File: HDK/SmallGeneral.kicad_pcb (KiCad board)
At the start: 2 copper layers, 80 x 50 mm, 45 parts, among them J101 PHD_02x04V-H, J102 USB_C, J103 PH_01x05V-H, J104 Conn_01x08, J105 PH_01x05V-H, J106 PH_01x05V-H, J107 PHD_02x04V-H, J108 PHD_02x04V-H, J109 Conn_01x08, SW101 SW_Push, SW102 SW_Push, U101 STM32F072CBTx, U102 TJA1042T-3, U103 AMS1117-3.3

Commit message: updated rev3
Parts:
- removed the G*** at (156.2, 122.5)
- removed H101, H102, H103, H104: MountingHole_4.3mm_M4_DIN965_Pad_TopBottom, MountingHole:MountingHole_4.3mm_M4_DIN965_Pad_TopBottom
- removed the J101 at (108.0, 132.6)
- removed J103, J105, J106: PH_01x05V-H, NVF-Kicad:PH_01x05H-H
- removed J104, J109: Conn_01x08, Connector_PinHeader_2.54mm:PinHeader_1x08_P2.54mm_Vertical
- removed J107, J108: PHD_02x04V-H, NVF-Kicad:PHD_02x04H-H
- removed SWD101: SWD_Breakout_Minimal, NVF-Kicad:PH_01x05H-H
- removed kibuzzard-65C10781: G***, kibuzzard-65C10781
- removed kibuzzard-65C107BB: G***, kibuzzard-65C107BB
- added C110: 100n, Capacitor_SMD:C_0603_1608Metric, F.Cu at (156.7, 138.5)
- added C113: 2u2, Capacitor_SMD:C_0805_2012Metric, F.Cu at (167.3, 118.9)
- added C114: 2u2, Capacitor_SMD:C_0805_2012Metric, F.Cu at (167.3, 116.6)
- added D101: GREEN, LED_SMD:LED_0603_1608Metric, F.Cu at (154.8, 133.3)
- added D102: RED, LED_SMD:LED_0603_1608Metric, F.Cu at (152.2, 133.3)
- added D103: BLUE, LED_SMD:LED_0603_1608Metric, F.Cu at (149.5, 133.3)
- added R103: 10k, Resistor_SMD:R_0603_1608Metric, F.Cu at (156.7, 140.2)
- added R104: 1k, Resistor_SMD:R_0603_1608Metric, F.Cu at (156.7, 141.8)
- added R105: 200, Resistor_SMD:R_0603_1608Metric, F.Cu at (154.7, 129.9)
- added R106: 200, Resistor_SMD:R_0603_1608Metric, F.Cu at (152.2, 129.9)
- added R107: 200, Resistor_SMD:R_0603_1608Metric, F.Cu at (149.5, 129.9)
- added R110: 10k, Resistor_SMD:R_0603_1608Metric, F.Cu at (160.8, 140.4)
- added R111: 1k, Resistor_SMD:R_0603_1608Metric, F.Cu at (160.8, 142.1)
- added RV102: 10k, NVF-Kicad:RV_Bourns_3362, F.Cu at (129.9, 121.9)
- added SG101: ~, NVF-OwnParts:Small-General Actual, F.Cu at (140.0, 125.0)
- added SW103: SW_Push, NVF-Kicad:PushBtn_TS-1187A-B-A-B, F.Cu at (159.8, 146.2)
- added TP102: TestPoint, TestPoint:TestPoint_Pad_2.5x2.5mm, F.Cu at (116.0, 110.4)
- added TP103: TestPoint, TestPoint:TestPoint_Pad_2.5x2.5mm, F.Cu at (177.2, 122.5)
- added U104: AMS1117-5.0, Package_TO_SOT_SMD:SOT-223-3_TabPin2, F.Cu at (173.9, 116.7)
- added kibuzzard-65CCCADD: G***, kibuzzard-65CCCADD, F.Cu at (164.2, 123.9)
- added kibuzzard-65CCCB35: G***, kibuzzard-65CCCB35, B.Cu at (139.3, 125.1)
- moved R101 8.88 mm to (128.6, 117.2), turned to 0 degrees
- moved D104 6.83 mm to (166.6, 138.2)
- moved C103 2.35 mm to (129.9, 128.3), turned to 180 degrees
- moved kibuzzard-65C10821 1.98 mm to (146.4, 135.0)
- moved kibuzzard-65C10836 1.98 mm to (144.0, 130.0)
- renumbered C111 to C109, C109 to C111, C110 to C112, D101 to D104, D102 to D105, D103 to D106, J102 to J101, R105 to R102, R103 to R108, R104 to R109
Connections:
- net BOOT0 renamed /BOOT0
- C109 pad 1: NRST -> /NRST
- R101 pad 1: NRST -> +3V3
- R101 pad 2: +3V3 -> /NRST
- SW102 pad 1: NRST -> /NRST
- U101 pad 10: unconnected-(U101-PA0-Pad10) -> /A0_MCU
- U101 pad 11: /A0_MCU -> /A1_MCU
- U101 pad 19: unconnected-(U101-PB1-Pad19) -> /V_{SENSE}
- U101 pad 20: unconnected-(U101-PB2-Pad20) -> /USR_BTN
- U101 pad 21: unconnected-(U101-PB10-Pad21) -> /USR_LED
- U101 pad 7: NRST -> /NRST
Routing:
- net NRST: track 71.4 -> 0.00 mm, vias 5 -> 0
- net /NRST: track 0.00 -> 68.1 mm, vias 0 -> 5
- net +5V: track 102.1 -> 154.3 mm, vias 2 -> 4
- net /A1_MCU: track 0.00 -> 43.8 mm, vias 0 -> 2
- net VCC: track 63.8 -> 98.5 mm, vias 2 -> 4
- net /USR_LED: track 0.00 -> 32.1 mm, vias 0 -> 2
- net /V_{SENSE}: track 0.00 -> 29.9 mm, vias 0 -> 2
- net /A1: track 0.00 -> 26.8 mm
- net /USR_BTN: track 0.00 -> 25.1 mm
- net Net-(R104-Pad2): track 0.00 -> 8.75 mm
- net VBUS: track 21.9 -> 14.6 mm
- net GND: track 44.8 -> 51.4 mm, vias 23 -> 35
- net +3V3: track 227.7 -> 233.8 mm, vias 8 -> 9
- net /SPI_MOSI: track 26.6 -> 21.1 mm
- net /SPI_SCLK: track 22.0 -> 18.0 mm
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- added copper zone on F.Cu, net +5V
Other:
- board text added: "3V3"
- board text added: "5V"
- board text added: "A0_T"
- board text added: "A1_T"
- board text added: "B"
- board text added: "BOOT"
- board text added: "G"
- board text added: "NRST"
- board text added: "Rev3"
- board text added: "Scott CJX NVF"
- board text added: "USR"
- board text removed: "A0"
- board text removed: "CAN"
- board text removed: "CAN INTR"
- board text removed: "I2C"
- board text removed: "Rev1"
- board text removed: "SPI"
- board text removed: "SWD"
- board text removed: "UART"

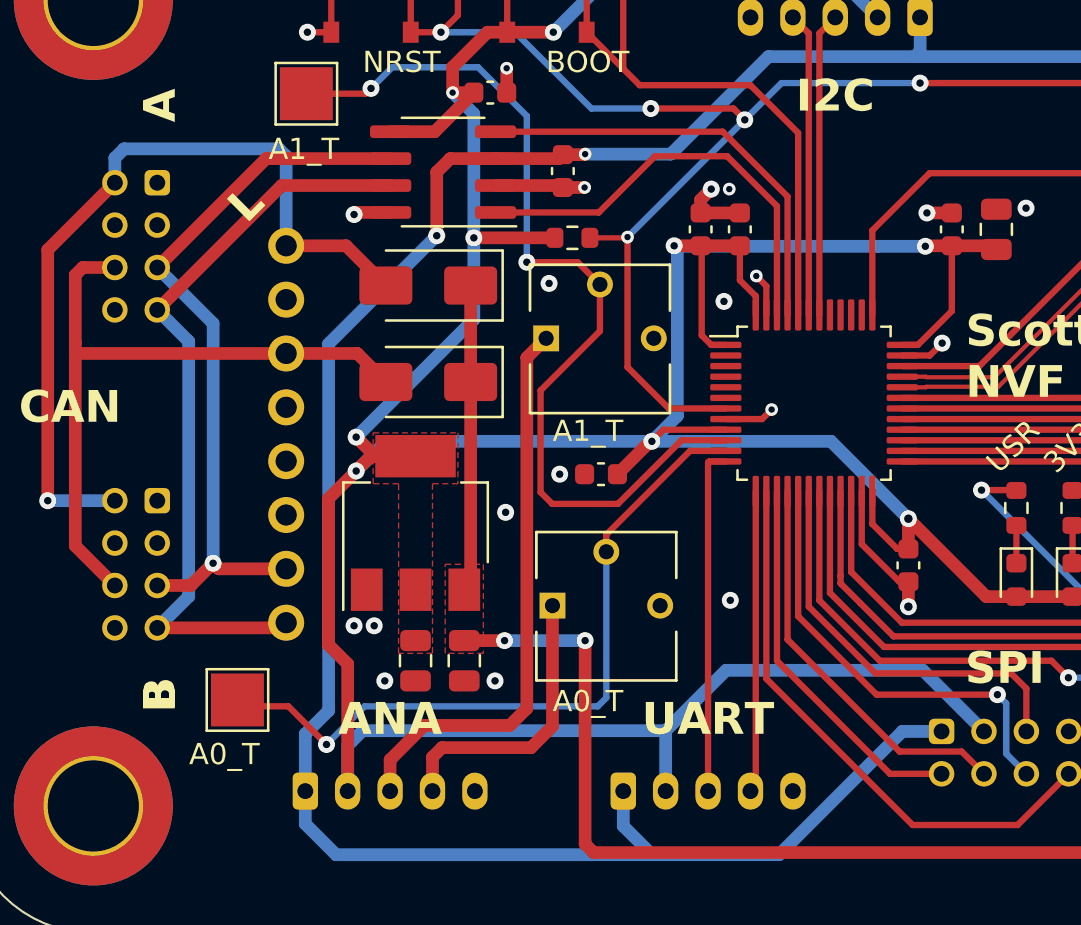
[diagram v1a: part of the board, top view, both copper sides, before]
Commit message: updated Trim Pot Switch
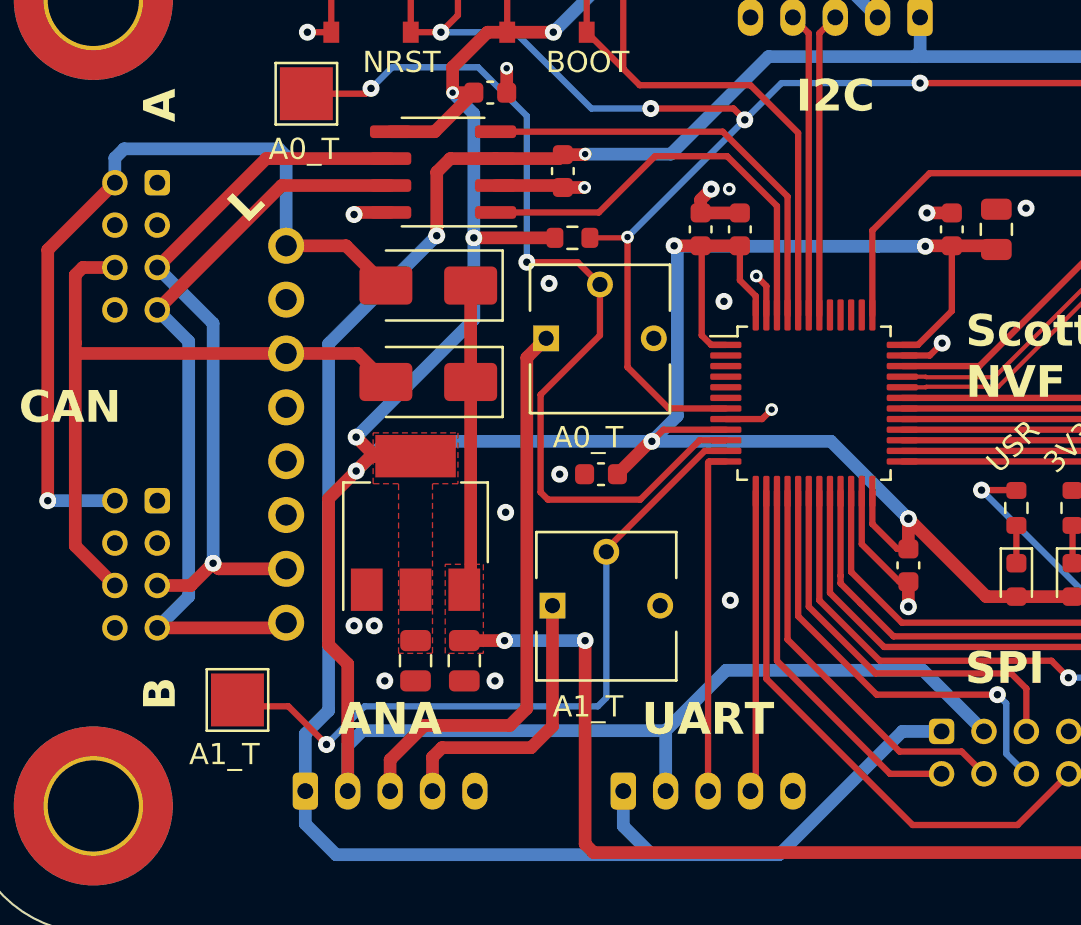
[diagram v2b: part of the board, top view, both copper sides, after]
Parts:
- renumbered RV102 to RV101, RV101 to RV102
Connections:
- RV101 pad 1: /A1 -> /A0
- RV101 pad 2: /A1_MCU -> /A0_MCU
- RV102 pad 1: /A0 -> /A1
- RV102 pad 2: /A0_MCU -> /A1_MCU
- SG101 pad G: (no net) -> GND
- TP101 pad 1: /A0_MCU -> /A1_MCU
- TP102 pad 1: /A1_MCU -> /A0_MCU
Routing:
- net /A1: track 26.8 -> 13.6 mm
- net /A0: track 13.6 -> 26.8 mm
- net /A1_MCU: track 43.8 -> 33.7 mm, vias 2 -> 1
- net /A0_MCU: track 34.2 -> 43.7 mm, vias 1 -> 2
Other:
- board text removed: "B"

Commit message: updated  docs
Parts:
- added F101: Fuse, NVF-Kicad:FUSE-Littelfuse_Nano2_154x, F.Cu at (108.5, 104.8)
- moved D105 20.1 mm to (104.2, 109.8)
- moved D106 16.0 mm to (114.5, 109.8), turned to 0 degrees
- moved TP102 5.81 mm to (116.3, 104.6)
- moved C109 2.00 mm to (125.2, 104.5)
- moved R102 2.00 mm to (133.0, 104.5)
- moved SW101 2.00 mm to (129.4, 104.5)
- moved SW102 2.00 mm to (121.1, 104.5)
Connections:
- D105 pad 1: VCC -> Net-(D105-K)
- D106 pad 1: VCC -> Net-(D105-K)
- SG101 pad E1: +5V -> unconnected-(SG101B-5V-PadE1)
- SG101 pad E2: +3V3 -> unconnected-(SG101B-3V3-PadE2)
- SG101 pad E3: /SPI_IRQ -> /SPI_MISO
- SG101 pad E5: /SPI_SCLK -> GND
- SG101 pad E6: /SPI_MISO -> +5V
- SG101 pad E7: /SPI_MOSI -> +3V3
- SG101 pad E8: /SPI_CS -> /SPI_SCLK
- SG101 pad G: GND -> (no net)
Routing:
- net VCC: track 98.5 -> 124.1 mm, vias 4 -> 6
- net +3V3: track 233.8 -> 245.8 mm, vias 9 -> 11
- net Net-(D105-K): track 0.00 -> 11.7 mm
- net V2: track 32.6 -> 41.4 mm, vias 0 -> 1
- net GND: track 51.4 -> 54.6 mm, vias 35 -> 36
- net /NRST: track 68.1 -> 66.1 mm
- net /BOOT0: track 30.4 -> 28.6 mm
- net /A0_MCU: track 43.7 -> 44.8 mm
- net V1: track 38.8 -> 39.6 mm
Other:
- board text added: "Rev4"
- board text removed: "Rev3"
